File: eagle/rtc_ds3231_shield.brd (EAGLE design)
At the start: 59.7 x 53.3 mm, 16 parts, among them U1 ARDUINO_SHIELDLABEL

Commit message: 2nd Initial Commit
Typo on the RTC Chip being used.
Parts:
- U$2: value DS3212 -> DS3231
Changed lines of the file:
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@@
 <element name="JP1" library="SparkFun" package="1X02" value="I2C_HDR" x="10.16" y="50.8" smashed="yes"/>
 <element name="JP2" library="SparkFun" package="1X02" value="IOREF" x="19.05" y="2.54" smashed="yes"/>
-<element name="U$2" library="Add-Ohms" package="SO16L" value="DS3212" x="41.91" y="29.21" smashed="yes" rot="R270">
+<element name="U$2" library="Add-Ohms" package="SO16L" value="DS3231" x="41.91" y="29.21" smashed="yes" rot="R270">
 <attribute name="VALUE" x="38.989" y="34.798" size="1.27" layer="27" ratio="10"/>
 </element>

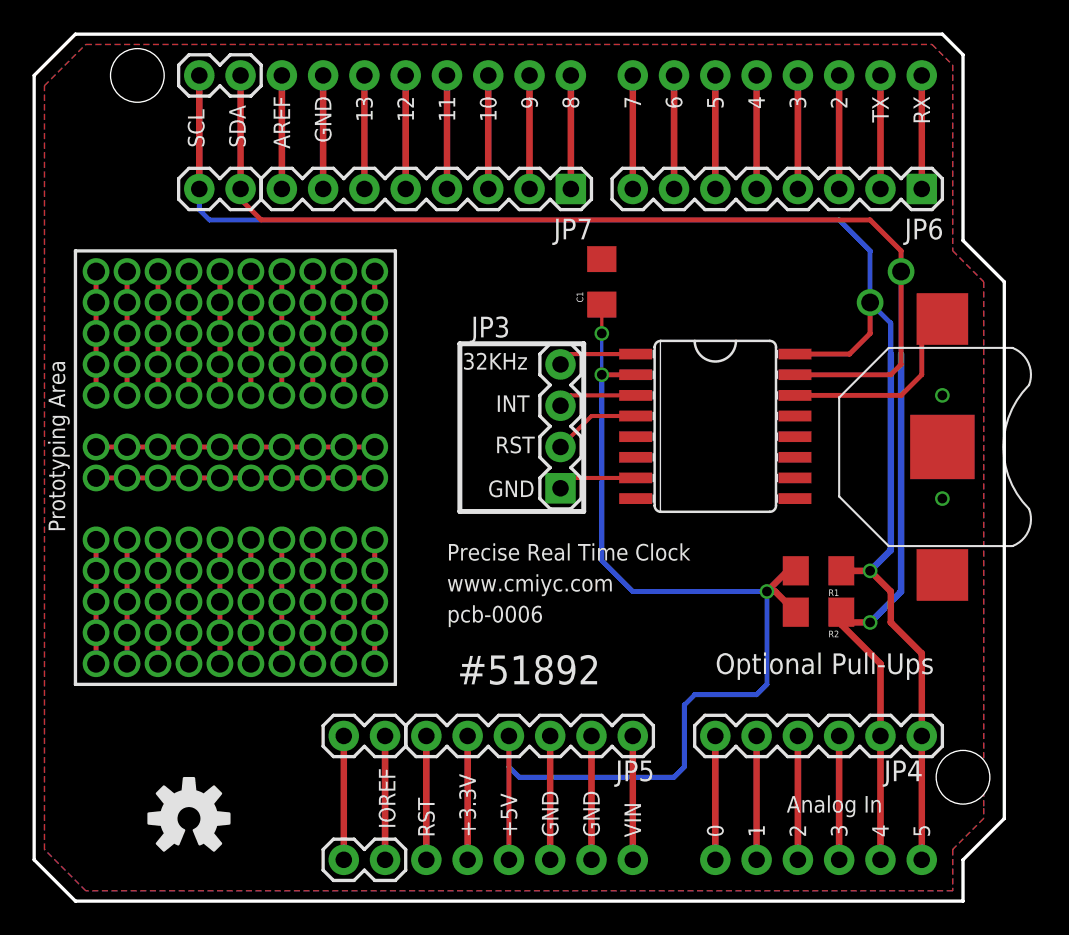
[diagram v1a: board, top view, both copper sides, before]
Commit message: Rev1b Updates
Added LED, RESET Button, some silk screen, cleaned up silkscreen on
back, made prototyping area clean with 0.1" spacing.
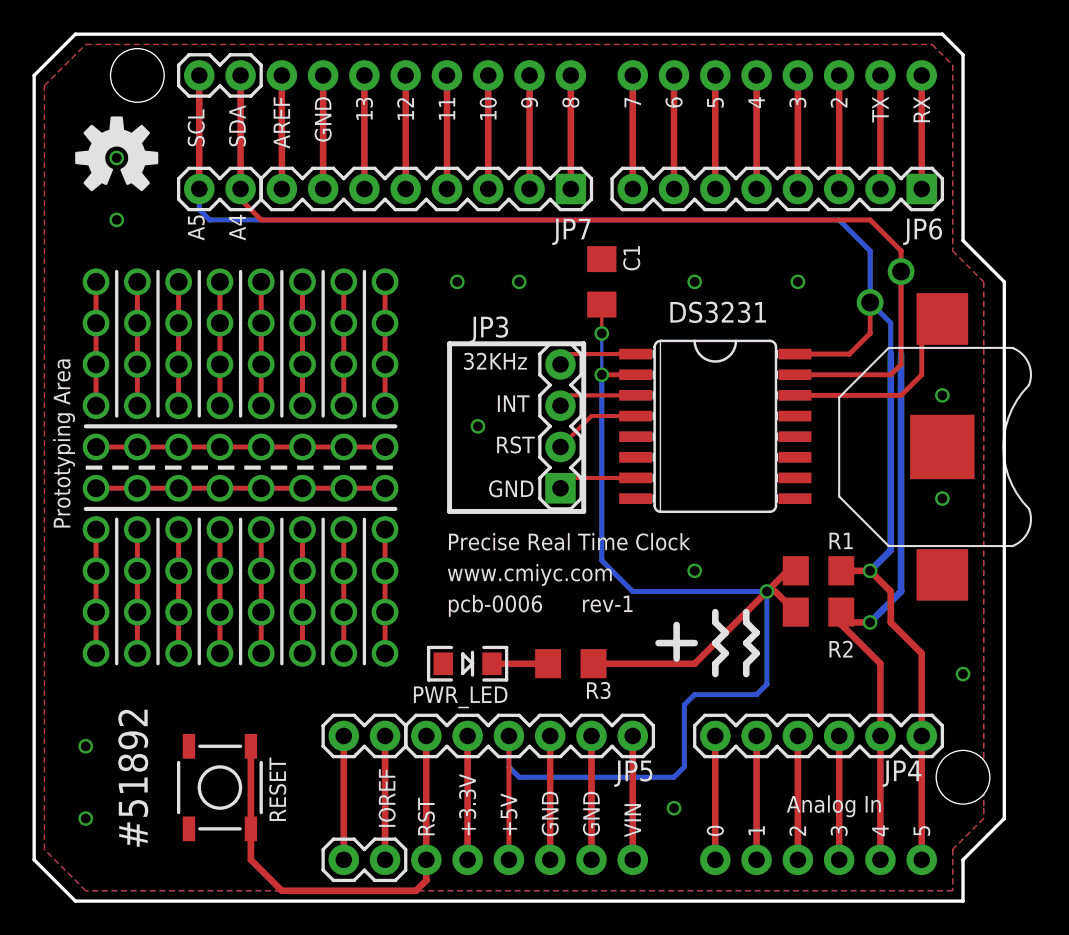
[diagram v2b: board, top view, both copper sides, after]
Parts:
- added PWR_LED: (no value), Add-Ohms:LED-1206
- added R3: 220, Add-Ohms:1206
- added RESET: (no value), Add-Ohms:TACTILE_SWITCH_SMD
- added U$3: OSHW-LOGOM, Add-Ohms:OSHW-LOGO-M
- C1: value (none) -> 1u
- R1, R2: value (none) -> 4k7
- moved U$1 40.9 mm to (5.08, 45.7)
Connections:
- new net N$5: PWR_LED.C, R3.2
- net GND: now also PWR_LED.A, RESET.3, RESET.4
- net RESET: now also RESET.1, RESET.2
- net VCC: now also R3.1
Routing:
- net RESET: track 7.62 -> 27.7 mm
- net N$97: track 15.2 -> 0.00 mm, vias 2 -> 0
- net N$92: track 15.2 -> 0.00 mm, vias 2 -> 0
- net N$27: track 15.2 -> 0.00 mm, vias 2 -> 0
- net VCC: track 70.5 -> 83.1 mm
- net N$5: track 15.2 -> 3.45 mm, vias 2 -> 0
- net N$91: track 34.3 -> 35.6 mm
- net N$90: track 34.3 -> 35.6 mm
- net N$141: vias 2 -> 1
- net N$136: vias 2 -> 1
- net N$131: vias 2 -> 1
- net N$122: vias 2 -> 1
- net N$117: vias 2 -> 1
- net N$116: vias 2 -> 1
- net N$107: vias 2 -> 1
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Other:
- board text added: "0"
- board text added: "1"
- board text added: "10"
- board text added: "11"
- board text added: "12"
- board text added: "13"
- board text added: "2"
- board text added: "3"
- board text added: "3V3"
- board text added: "4"
- board text added: "5"
- board text added: "5V"
- board text added: "6"
- board text added: "7"
- board text added: "8"
- board text added: "9"
- board text added: "A4"
- board text added: "A5"
- board text added: "AREF"
- board text added: "JP3"
- board text added: "JP4"
- board text added: "JP5"
- board text added: "JP6"
- board text added: "JP7"
- board text added: "VIN"
- board text added: "gnd"
- board text added: "rev-1"
- board text removed: "Columns Are Connected"
- board text removed: "Optional Pull-Ups"
- board text removed: "Rows Connected Together"
- board text removed: "Traces on Top and Bottom"

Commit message: Minor changes
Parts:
- moved U$3 40.8 mm to (5.08, 45.7)
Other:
- board text added: "#61467"
- board text added: "addohms.com"
- board text removed: "#51892"
- board text removed: "James Lews"
- board text removed: "byerly0503@gmail.com"
- board text removed: "www.cmiyc.com"
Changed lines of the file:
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@@
 <?xml version="1.0" encoding="utf-8"?>
 <!DOCTYPE eagle SYSTEM "eagle.dtd">
-<eagle version="6.0">
+<eagle version="6.3">
 <drawing>
 <settings>
@@
 <wire x1="57.15" y1="0" x2="2.54" y2="0" width="0.2032" layer="20"/>
 <wire x1="2.54" y1="0" x2="0" y2="2.54" width="0.2032" layer="20"/>
-<text x="25.4" y="19.685" size="1.016" layer="25" font="fixed">www.cmiyc.com</text>
-<text x="25.4" y="17.78" size="1.016" layer="25" font="fixed">pcb-0006</text>
-<text x="41.91" y="20.32" size="1.016" layer="26" font="fixed" rot="MR0">James Lews</text>
-<text x="41.91" y="19.05" size="1.016" layer="26" font="fixed" rot="MR0">byerly0503@gmail.com</text>
-<text x="25.4" y="21.59" size="1.016" layer="25" font="fixed">Precise Real Time Clock</text>
+<text x="26.035" y="19.685" size="1.016" layer="25" font="fixed">pcb-0006</text>
+<text x="22.225" y="12.7" size="1.016" layer="26" font="fixed" rot="MR0">Precise Real Time Clock</text>
 <wire x1="3.175" y1="24.13" x2="22.225" y2="24.13" width="0.254" layer="26"/>
-<text x="6.985" y="3.175" size="1.778" layer="25" rot="R90">#51892</text>
+<text x="5.715" y="2.54" size="1.778" layer="26" rot="MR90">#61467</text>
 <wire x1="7.62" y1="14.605" x2="7.62" y2="23.495" width="0.2032" layer="25"/>
 <wire x1="10.16" y1="14.605" x2="10.16" y2="23.495" width="0.2032" layer="25"/>
@@
 <wire x1="33.81375" y1="23.97125" x2="33.81375" y2="34.29" width="0.3048" layer="26"/>
 <wire x1="25.55875" y1="23.97125" x2="33.81375" y2="23.97125" width="0.3048" layer="26"/>
-<text x="33.655" y="17.78" size="1.016" layer="25" font="fixed">rev-1</text>
+<text x="14.605" y="11.43" size="1.016" layer="26" font="fixed" rot="MR0">rev-1</text>
 <text x="36.5125" y="48.5775" size="1.016" layer="26" font="fixed" rot="MR90">7</text>
 <text x="39.0525" y="48.5775" size="1.016" layer="26" font="fixed" rot="MR90">6</text>
@@
 <circle x="34.925" y="32.385" radius="0.15" width="0.3" layer="116"/>
 <circle x="34.925" y="34.925" radius="0.15" width="0.3" layer="116"/>
+<text x="26.035" y="20.955" size="1.27" layer="21">addohms.com</text>
 </plain>
 <attributes>
@@
 </class>
 </classes>
-<designrules>
+<designrules name="default">
 <description language="de">&lt;b&gt;EAGLE Design Rules&lt;/b&gt;
 &lt;p&gt;
@@
 <attribute name="VALUE" x="36.449" y="36.703" size="0.4064" layer="27" rot="R90"/>
 </element>
-<element name="U$3" library="Add-Ohms" package="OSHW-LOGO-M" value="OSHW-LOGOM" x="13.335" y="5.715" rot="MR0"/>
+<element name="U$3" library="Add-Ohms" package="OSHW-LOGO-M" value="OSHW-LOGOM" x="5.08" y="45.72" rot="MR0"/>
 <element name="RESET" library="Add-Ohms" package="TACTILE_SWITCH_SMD" value="" x="11.43" y="6.985" smashed="yes" rot="R270">
 <attribute name="NAME" x="14.478" y="8.8265" size="1.016" layer="25" font="fixed" rot="R270"/>
@@
 </element>
 <element name="PWR_LED" library="Add-Ohms" package="LED-1206" value="" x="26.67" y="14.605" smashed="yes">
-<attribute name="NAME" x="23.241" y="12.192" size="1.016" layer="25"/>
+<attribute name="NAME" x="26.416" y="16.002" size="1.016" layer="25"/>
 <attribute name="VALUE" x="25.654" y="12.827" size="0.4064" layer="27"/>
 </element>
